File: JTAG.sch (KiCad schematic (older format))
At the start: 2 parts, among them CN5 CONN_RCPT_USB2.0_MINI_B_SMD_R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, U15 FT2232HL-REEL

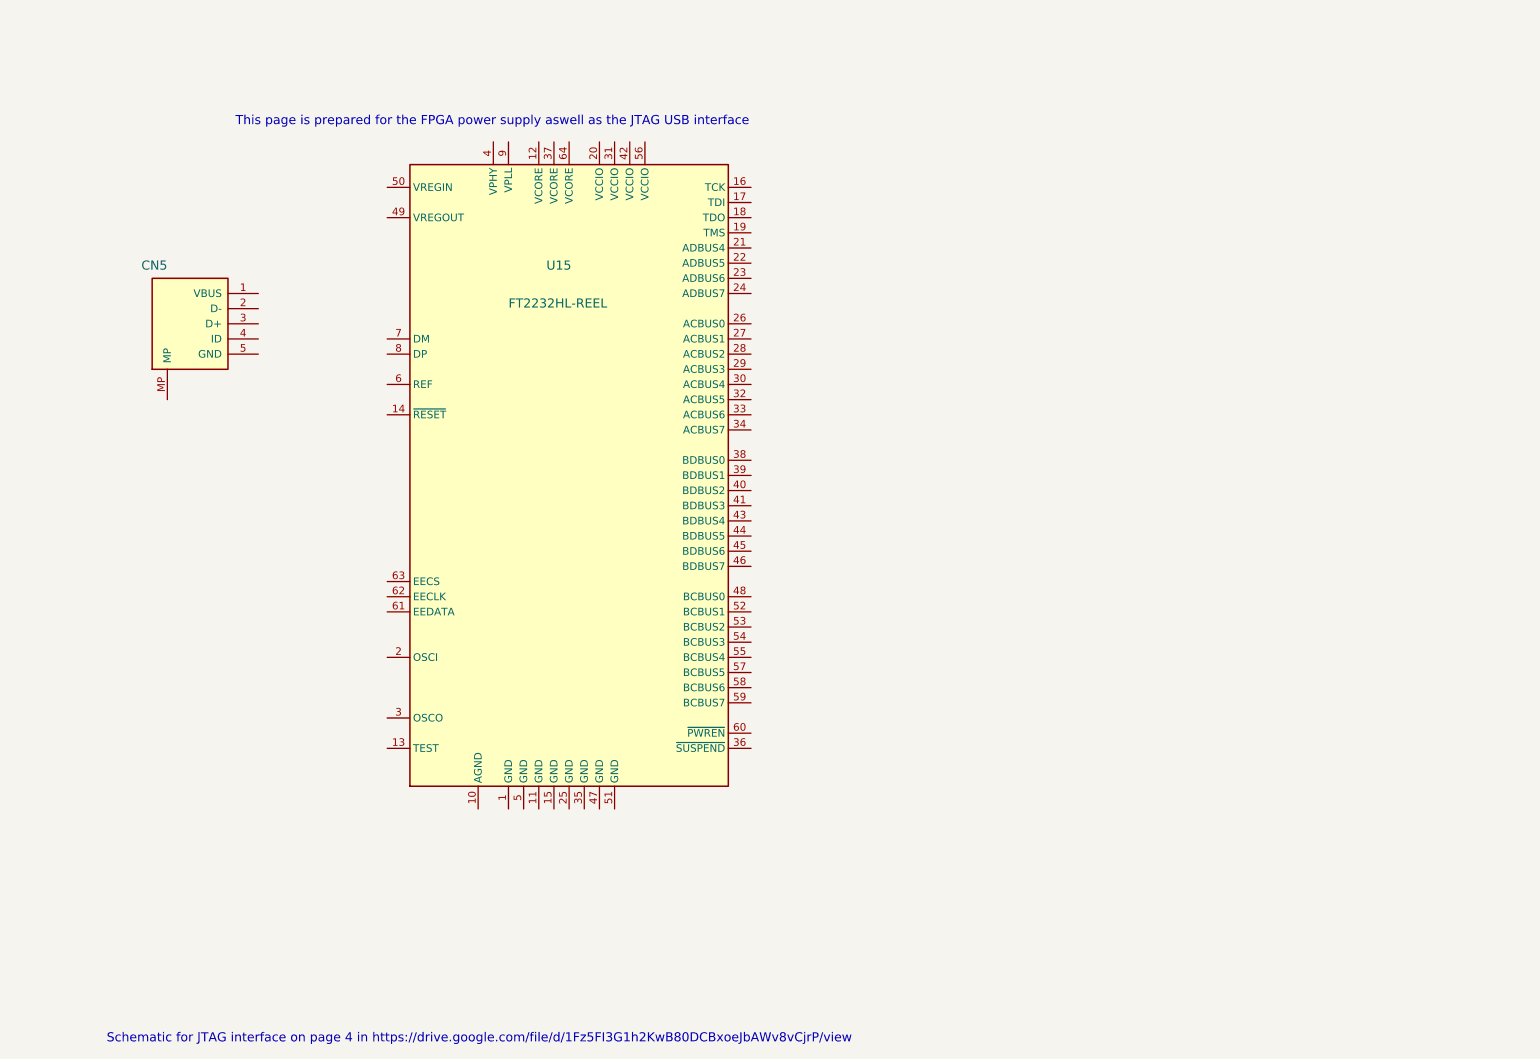
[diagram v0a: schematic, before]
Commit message: Continuing on with library updates.  Started to fix up the USB interfaces.
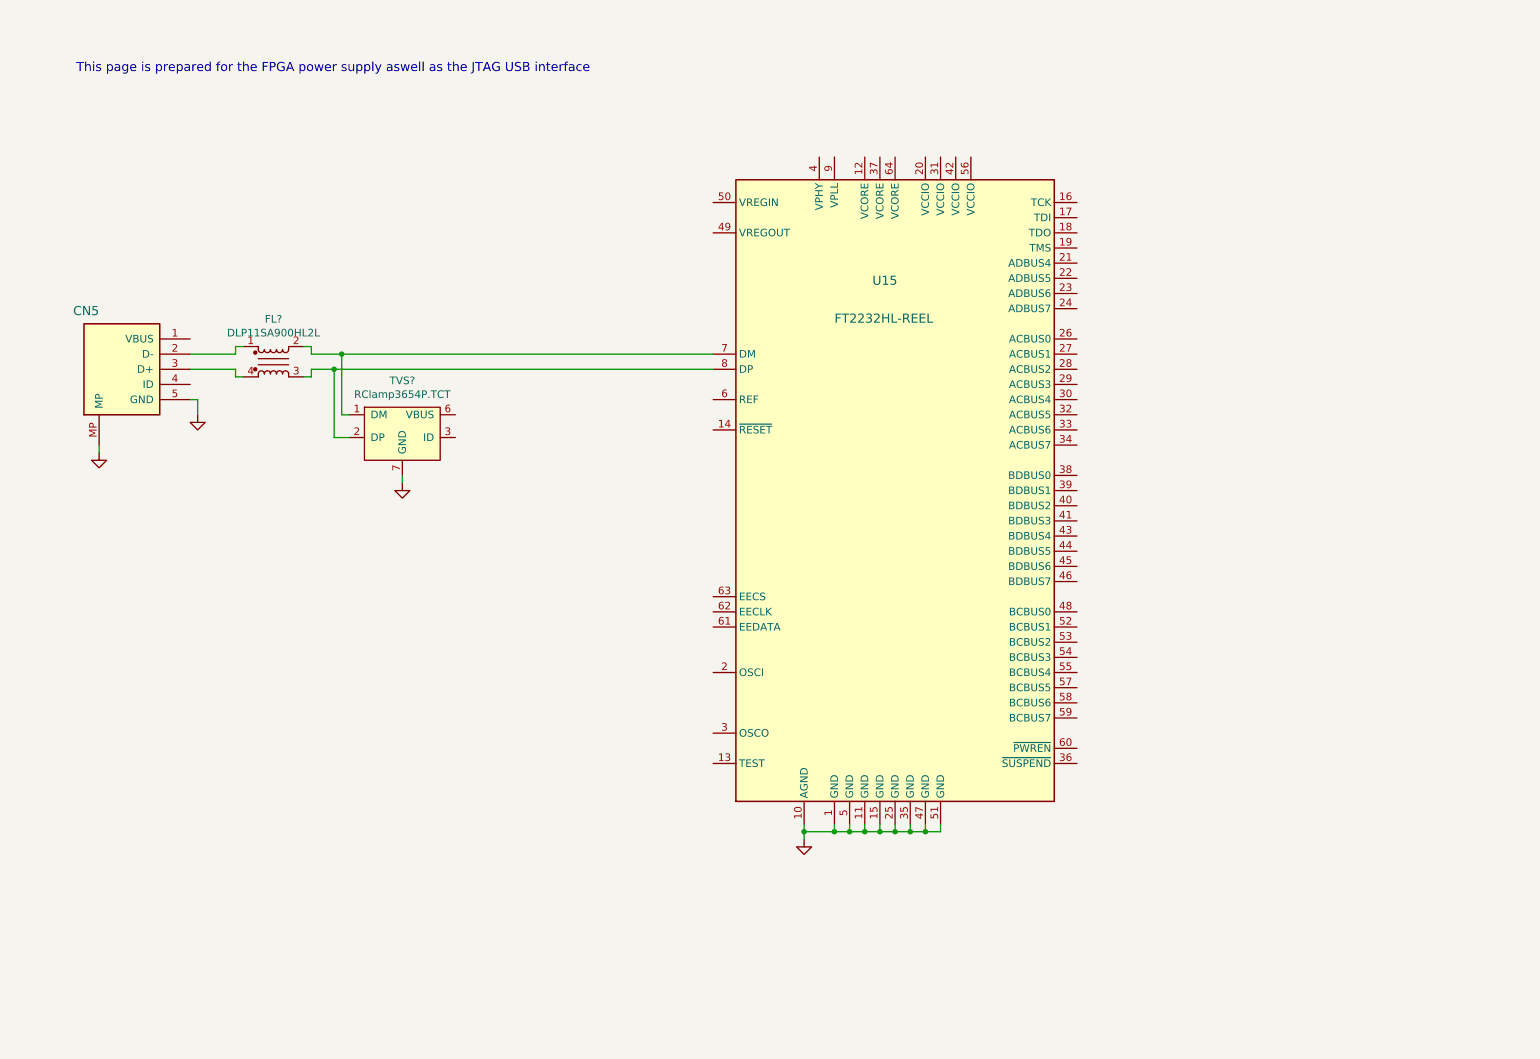
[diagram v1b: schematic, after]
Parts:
- added FL?: DLP11SA900HL2L, F_Inductors:Murata_DLP11S, symbol F_inductors:DLP11SA900HL2L
- added TVS?: RClamp3654P.TCT, F_Misc:SON50P160X160X65-7N, symbol F_Misc:RClamp3654P.TCT
- U15: footprint (none) -> Package_QFP:LQFP-64_10x10mm_P0.5mm; Desc (none) -> IC USB HS DUAL UART/FIFO 64-LQFP; Detailed (none) -> USB Bridge, USB to UART,FIFO USB 2.0 UART Interface 64-LQFP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; DistName (none) -> DigiKey; Dist_PN (none) -> 768-1024-2-ND; Mfr (none) -> FTDI, Future Technology Devices International Ltd; Mfr_PN (none) -> FT2232HL-REEL
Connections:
- net GND: now reaches U15.1 (GND)
- net GND: now also CN5.5 (GND), CN5.MP, U15.10 (AGND), U15.11 (GND), U15.15 (GND), U15.25 (GND), U15.35 (GND), U15.47 (GND), U15.5 (GND), U15.51 (GND), TVS?.7 (GND)
- net at U15.7 (DM): now also FL?.2, TVS?.1 (DM)
- net at U15.8 (DP): now also FL?.3, TVS?.2 (DP)
- net at CN5.2 (D-): now also FL?.1
- net at CN5.3 (D+): now also FL?.4
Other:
- note removed: "Schematic for JTAG interface on page 4 in https://drive.google.com/file/d/1Fz5FI3G1h2KwB80DCBxoeJbAWv8vCjrP/view"
- moved on the sheet: CN5, U15
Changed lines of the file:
@@
 Comment4 ""
 $EndDescr
-Text Notes 1650 1000 0    60   ~ 0
+Text Notes 600  650  0    60   ~ 0
 This page is prepared for the FPGA power supply aswell as the JTAG USB interface
-Text Notes 800  7050 0    60   ~ 0
-Schematic for JTAG interface on page 4 in https://drive.google.com/file/d/1Fz5FI3G1h2KwB80DCBxoeJbAWv8vCjrP/view
 $Comp
 L OpenVent:CONN_RCPT_USB2.0_MINI_B_SMD_R_A CN5
 U 1 1 5F8DD18A
-P 1800 2500
-F 0 "CN5" H 2400 3050 60  0000 L BNN
-F 1 "CONN_RCPT_USB2.0_MINI_B_SMD_R_A" H 1800 2500 60  0001 C CNN
-F 2 "" H 1800 2500 60  0001 C CNN
-F 3 "" H 1800 2500 60  0001 C CNN
-	1    1800 2500
+P 1350 2800
+F 0 "CN5" H 1950 3350 60  0000 L BNN
+F 1 "CONN_RCPT_USB2.0_MINI_B_SMD_R_A" H 1350 2800 60  0001 C CNN
+F 2 "" H 1350 2800 60  0001 C CNN
+F 3 "" H 1350 2800 60  0001 C CNN
+	1    1350 2800
 	-1   0    0    -1
 $EndComp
@@
 L OpenVent:FT2232HL-REEL U15
 U 1 1 5F8DD189
-P 3850 3300
-F 0 "U15" H 3700 4650 60  0000 L BNN
-F 1 "FT2232HL-REEL" H 3450 4400 60  0000 L BNN
-F 2 "" H 6070 3200 60  0000 C CNN
-F 3 "" H 6070 3200 60  0000 C CNN
-	1    3850 3300
+P 6000 3400
+F 0 "U15" H 5850 4750 60  0000 L BNN
+F 1 "FT2232HL-REEL" H 5600 4500 60  0000 L BNN
+F 2 "Package_QFP:LQFP-64_10x10mm_P0.5mm" H 8220 3300 60  0001 C CNN
+F 3 "https://www.ftdichip.com/Support/Documents/DataSheets/ICs/DS_FT2232H.pdf" H 8220 3300 60  0001 C CNN
+F 4 "IC USB HS DUAL UART/FIFO 64-LQFP" H 6000 3400 50  0001 C CNN "Desc"
+F 5 "USB Bridge, USB to UART,FIFO USB 2.0 UART Interface 64-LQFP (10x10)" H 6000 3400 50  0001 C CNN "Detailed"
+F 6 "DigiKey" H 6000 3400 50  0001 C CNN "DistName"
+F 7 "768-1024-2-ND" H 6000 3400 50  0001 C CNN "Dist_PN"
+F 8 "FTDI, Future Technology Devices International Ltd" H 6000 3400 50  0001 C CNN "Mfr"
+F 9 "FT2232HL-REEL" H 6000 3400 50  0001 C CNN "Mfr_PN"
+	1    6000 3400
 	1    0    0    -1
 $EndComp
+$Comp
+L OpenVent:GND #PWR?
+U 1 1 5FB67287
+P 750 3150
+F 0 "#PWR?" H 750 2900 50  0001 C CNN
+F 1 "GND" H 750 3000 50  0001 C CNN
+F 2 "" H 750 3150 50  0001 C CNN
+F 3 "" H 750 3150 50  0001 C CNN
+	1    750  3150
+	1    0    0    -1
+$EndComp
+$Comp
+L OpenVent:GND #PWR?
+U 1 1 5FB678CE
+P 1400 2900
+F 0 "#PWR?" H 1400 2650 50  0001 C CNN
+F 1 "GND" H 1400 2750 50  0001 C CNN
+F 2 "" H 1400 2900 50  0001 C CNN
+F 3 "" H 1400 2900 50  0001 C CNN
+	1    1400 2900
+	1    0    0    -1
+$EndComp
+$Comp
+L F_Misc:RClamp3654P.TCT TVS?
+U 1 1 5FB67D83
+P 2750 3200
+F 0 "TVS?" H 2750 3725 50  0000 C CNN
+F 1 "RClamp3654P.TCT" H 2750 3634 50  0000 C CNN
+F 2 "F_Misc:SON50P160X160X65-7N" H 2750 3200 50  0001 C CNN
+F 3 "https://semtech.my.salesforce.com/sfc/p/E0000000JelG/a/44000000MCXN/wh6ib8C76Sfz_._po4NLxIgDm.uk2W3aErWuo281nzw" H 2750 3200 50  0001 C CNN
+F 4 "Semtech Corporation" H 2750 3200 50  0001 C CNN "Mfr"
+F 5 "RCLAMP3654P.TCT" H 2750 3200 50  0001 C CNN "Mfr_PN"
+F 6 "DigiKey" H 2750 3200 50  0001 C CNN "DistName"
+F 7 "RCLAMP3654P.TTR-ND" H 2750 3200 50  0001 C CNN "Dist_PN"
+F 8 "TVS DIODE 5.5V 30V SLP1616P6" H 2750 3200 50  0001 C CNN "Desc"
+F 9 "30V Clamp 3A (8/20µs) Ipp Tvs Diode Surface Mount SLP1616P6 (1.6x1.6)" H 2750 3200 50  0001 C CNN "Detailed"
+	1    2750 3200
+	1    0    0    -1
+$EndComp
+$Comp
+L F_inductors:DLP11SA900HL2L FL?
+U 1 1 5FB69009
+P 1900 2550
+F 0 "FL?" H 1900 2831 50  0000 C CNN
+F 1 "DLP11SA900HL2L" H 1900 2740 50  0000 C CNN
+F 2 "F_Inductors:Murata_DLP11S" H 1900 2590 50  0001 C CNN
+F 3 "https://media.digikey.com/pdf/Data%20Sheets/Murata%20PDFs/DLx_Series.pdf" H 1900 2590 50  0001 C CNN
+	1    1900 2550
+	1    0    0    -1
+$EndComp
+$Comp
+L OpenVent:GND #PWR?
+U 1 1 5FB6A55D
+P 2750 3350
+F 0 "#PWR?" H 2750 3100 50  0001 C CNN
+F 1 "GND" H 2750 3200 50  0001 C CNN
+F 2 "" H 2750 3350 50  0001 C CNN
+F 3 "" H 2750 3350 50  0001 C CNN
+	1    2750 3350
+	1    0    0    -1
+$EndComp
+Wire Wire Line
+	750  3100 750  3150
+Wire Wire Line
+	1350 2800 1400 2800
+Wire Wire Line
+	1400 2800 1400 2900
+Wire Wire Line
+	1350 2500 1650 2500
+Wire Wire Line
+	1650 2500 1650 2450
+Wire Wire Line
+	1650 2450 1700 2450
+Wire Wire Line
+	1350 2600 1650 2600
+Wire Wire Line
+	1650 2600 1650 2650
+Wire Wire Line
+	1650 2650 1700 2650
+Wire Wire Line
+	2100 2450 2150 2450
+Wire Wire Line
+	2150 2450 2150 2500
+Wire Wire Line
+	2150 2500 2350 2500
+Wire Wire Line
+	2100 2650 2150 2650
+Wire Wire Line
+	2150 2650 2150 2600
+Wire Wire Line
+	2150 2600 2300 2600
+Wire Wire Line
+	2400 2900 2350 2900
+Wire Wire Line
+	2350 2900 2350 2500
+Connection ~ 2350 2500
+Wire Wire Line
+	2400 3050 2300 3050
+Wire Wire Line
+	2300 3050 2300 2600
+Connection ~ 2300 2600
+Wire Wire Line
+	2750 3300 2750 3350
+Wire Wire Line
+	2350 2500 4800 2500
+Wire Wire Line
+	2300 2600 4800 2600
+$Comp
+L OpenVent:GND #PWR?
+U 1 1 5FB6D9F9
+P 5400 5700
+F 0 "#PWR?" H 5400 5450 50  0001 C CNN
+F 1 "GND" H 5400 5550 50  0001 C CNN
+F 2 "" H 5400 5700 50  0001 C CNN
+F 3 "" H 5400 5700 50  0001 C CNN
+	1    5400 5700
+	1    0    0    -1
+$EndComp
+Wire Wire Line
+	6300 5600 6300 5650
+Wire Wire Line
+	6300 5650 6200 5650
+Wire Wire Line
+	5400 5650 5400 5700
+Wire Wire Line
+	5400 5600 5400 5650
+Connection ~ 5400 5650
+Wire Wire Line
+	5600 5600 5600 5650
+Connection ~ 5600 5650
+Wire Wire Line
+	5600 5650 5400 5650
+Wire Wire Line
+	5700 5600 5700 5650
+Connection ~ 5700 5650
+Wire Wire Line
+	5700 5650 5600 5650
+Wire Wire Line
+	5800 5600 5800 5650
+Connection ~ 5800 5650
+Wire Wire Line
+	5800 5650 5700 5650
+Wire Wire Line
+	5900 5600 5900 5650
+Connection ~ 5900 5650
+Wire Wire Line
+	5900 5650 5800 5650
+Wire Wire Line
+	6000 5650 6000 5600
+Connection ~ 6000 5650
+Wire Wire Line
+	6000 5650 5900 5650
+Wire Wire Line
+	6100 5600 6100 5650
+Connection ~ 6100 5650
+Wire Wire Line
+	6100 5650 6000 5650
+Wire Wire Line
+	6200 5600 6200 5650
+Connection ~ 6200 5650
+Wire Wire Line
+	6200 5650 6100 5650
 $EndSCHEMATC

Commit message: Put USB to JTAG page together, first cut.
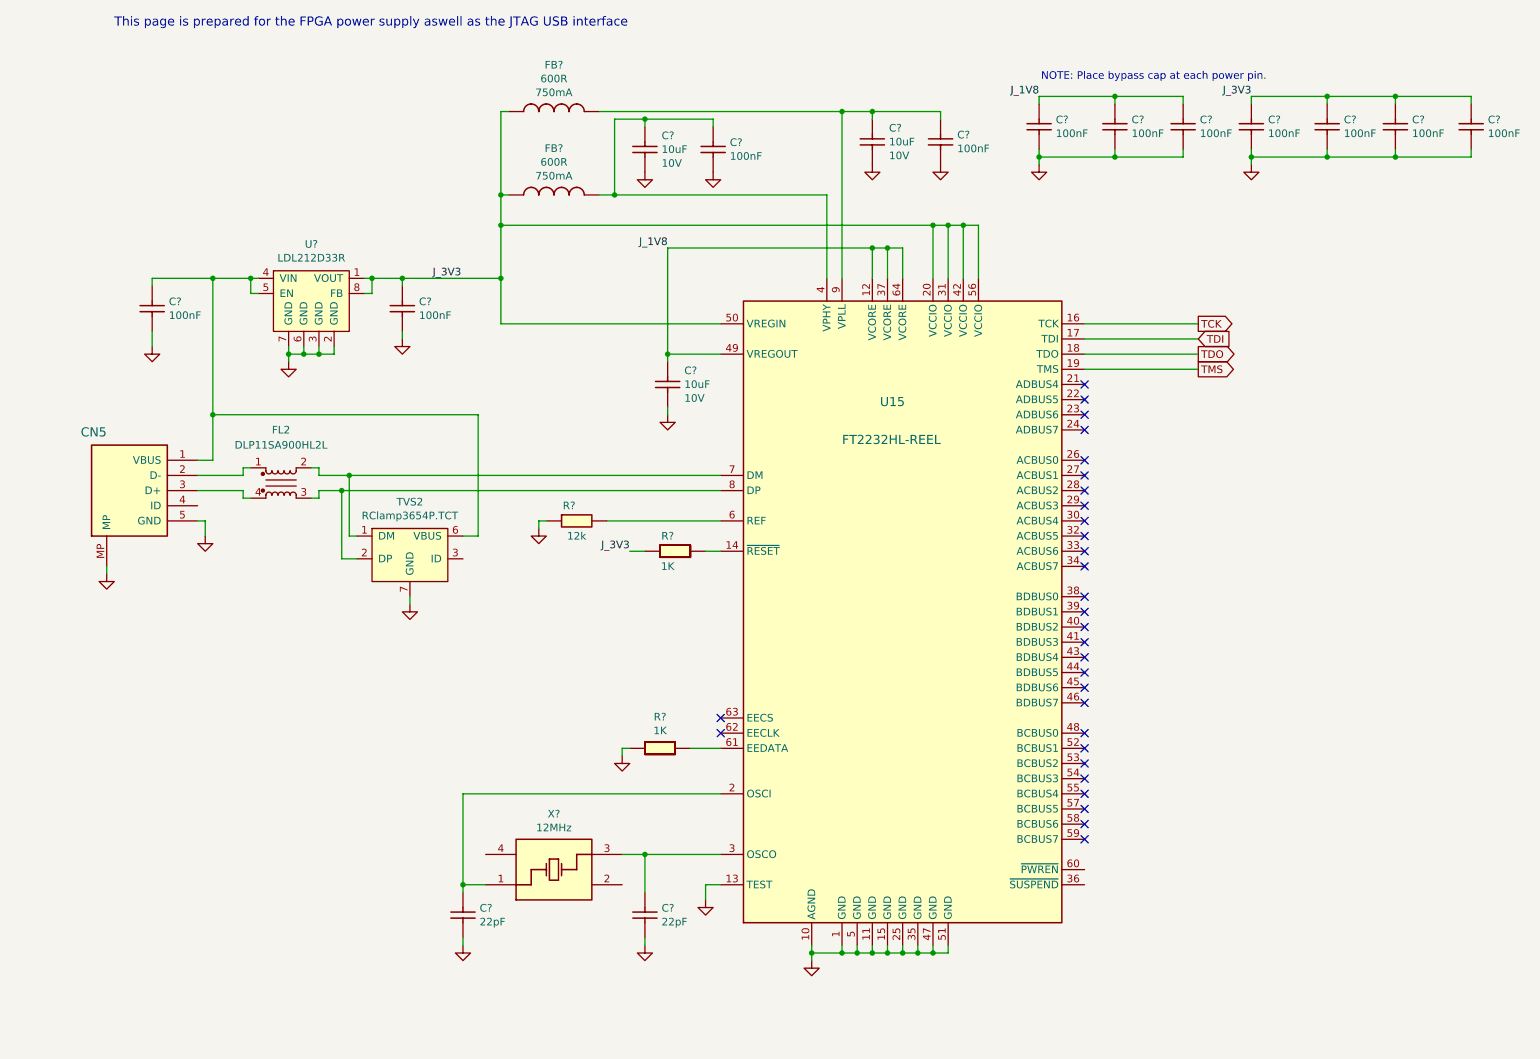
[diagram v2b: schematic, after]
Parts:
- added C? (x11): 100nF_0603_Ceramic_Capacitor,_10%,_X7R,_25V, symbol OpenVent:100nF_0603_Ceramic_Capacitor,_10%,_X7R,_25V
- added C? (x3): 10uF_0805_Ceramic_Capacitor_10%_X7R_10V, Capacitor_SMD:C_0805_2012Metric, symbol OpenVent:10uF_0805_Ceramic_Capacitor_10%_X7R_10V
- added C? (x2): 22pF_0603_Ceramic_Capacitor,_5%,_NP0,_50V, symbol OpenVent:22pF_0603_Ceramic_Capacitor,_5%,_NP0,_50V
- added FB? (x2): Chip_Ferrite,_600R,_0603,_750mA, symbol OpenVent:Chip_Ferrite,_600R,_0603,_750mA
- added R? (x2): 1K_0603_Chip_Resistor,_1%,_0.1W, symbol OpenVent:1K_0603_Chip_Resistor,_1%,_0.1W
- added R?: 12k_0603_Chip_Resistor,_1%,_0.1W, Resistor_SMD:R_0603_1608Metric, symbol OpenVent:12k_0603_Chip_Resistor,_1%,_0.1W
- added U?: LDL212D33R, Package_SO:SO-8_5.3x6.2mm_P1.27mm, symbol OpenVent:LDL212D33R
- added X?: ABM3B-12.000MHZ, Crystal:Crystal_SMD_Abracon_ABM3B-4Pin_5.0x3.2mm, symbol OpenVent:ABM3B-12.000MHZ
- gave numbers to parts that had none: 2
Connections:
- net GND: now also U15.13 (TEST), C?.2, C?.2, C?.2, C?.2, C?.2, C?.2, C?.2, C?.2, C?.2, C?.2, C?.2, C?.2, C?.2, C?.2, C?.2, C?.2, R?.1, R?.1, U?.2 (GND), U?.3 (GND), U?.6 (GND), U?.7 (GND)
- net J_1V8: now reaches U15.12 (VCORE)
- net J_1V8: now also U15.37 (VCORE), U15.49 (VREGOUT), U15.64 (VCORE), C?.1, C?.1, C?.1, C?.1
- net at U15.14 (~RESET): now also R?.2
- net TCK: now reaches U15.16 (TCK)
- net TDI: now reaches U15.17 (TDI)
- net TDO: now reaches U15.18 (TDO)
- net TMS: now reaches U15.19 (TMS)
- net at U15.2 (OSCI): now also C?.1, X?.1 (OSC1)
- net J_3V3: now reaches U15.20 (VCCIO)
- net J_3V3: now also U15.31 (VCCIO), U15.42 (VCCIO), U15.50 (VREGIN), U15.56 (VCCIO), C?.1, C?.1, C?.1, C?.1, C?.1, FB?.1, FB?.1, R?.1, U?.1 (VOUT), U?.8 (FB)
- net at U15.3 (OSCO): now also C?.1, X?.3 (OSC3)
- net at U15.4 (VPHY): now also C?.1, C?.1, FB?.2
- net at U15.6 (REF): now also R?.2
- net at U15.61 (EEDATA): now also R?.2
- net at U15.9 (VPLL): now also C?.1, C?.1, FB?.2
- net at CN5.1 (VBUS): now also TVS2.6 (VBUS), C?.1, U?.4 (VIN), U?.5 (EN)
- no-connect marks 0 -> 30
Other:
- note added: "NOTE: Place bypass cap at each power pin."
- moved on the sheet: CN5, FL2, TVS2, U15

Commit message: Added in 8 RGB LEDs for the UI.
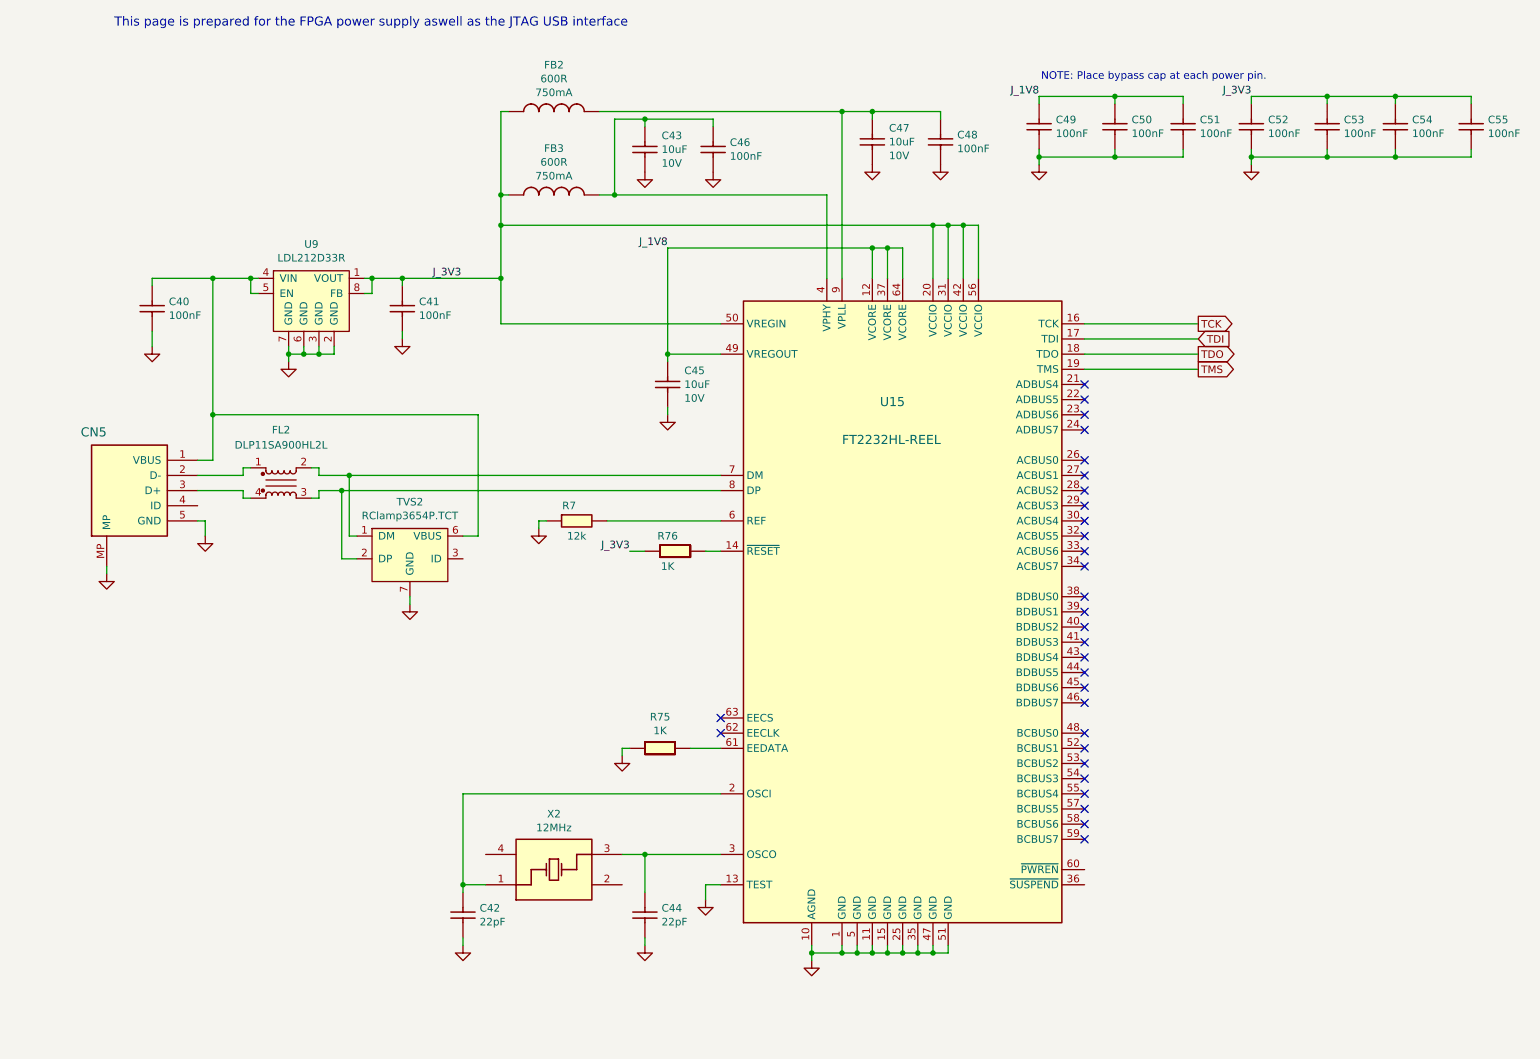
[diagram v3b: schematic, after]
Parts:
- gave numbers to parts that had none: 23
